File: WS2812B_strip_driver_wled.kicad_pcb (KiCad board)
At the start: 2 copper layers, 112.9 x 106.2 mm, 119 parts, among them J1 CH_1, J2 CH_2, J3 CH_3, J4 CH_4, J5 PWR_IN, J6 uPhone, J8 USB_C_Receptacle_USB2.0_16P, K1 RELAY_1, K2 RELAY_2, K3 RELAY_3, K4 RELAY_4, Q1 SS8050, Q2 SS8050, Q3 SS8050, Q4 SS8050, Q5 SS8050, Q6 SS8050, SW1 SW_EN, SW2 SW_IO0, U1 ESP32-WROOM-32E, U2 AMS1117-3.3, U3 CP2102N-Axx-xQFN28

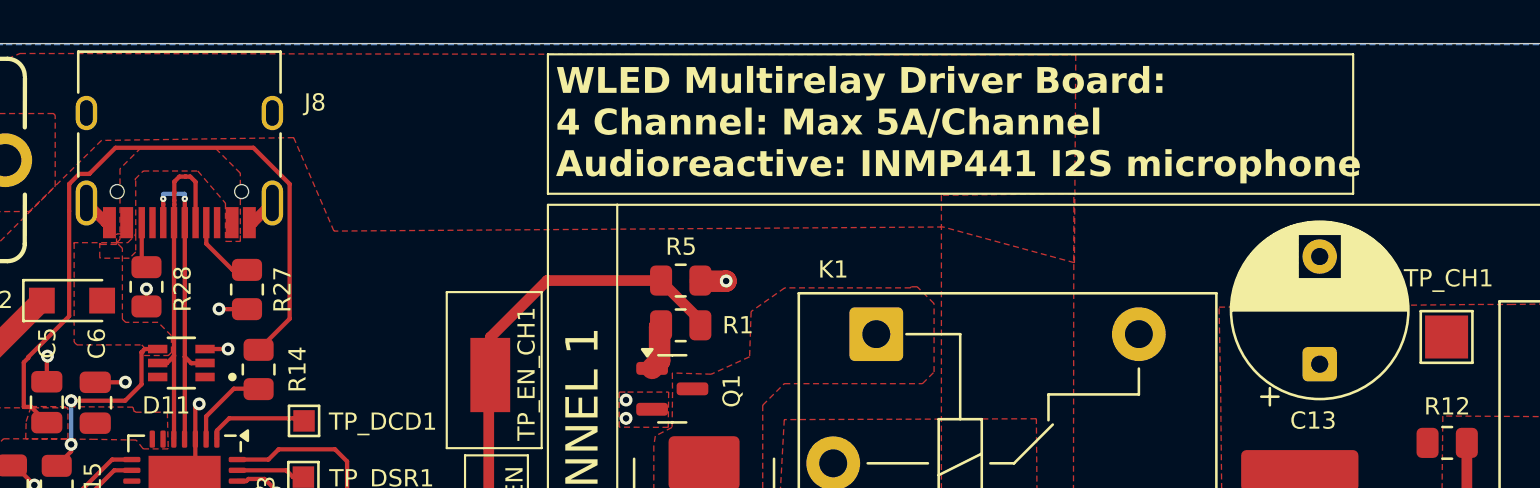
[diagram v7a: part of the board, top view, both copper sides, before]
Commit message: removed micro vias by usb-c connection
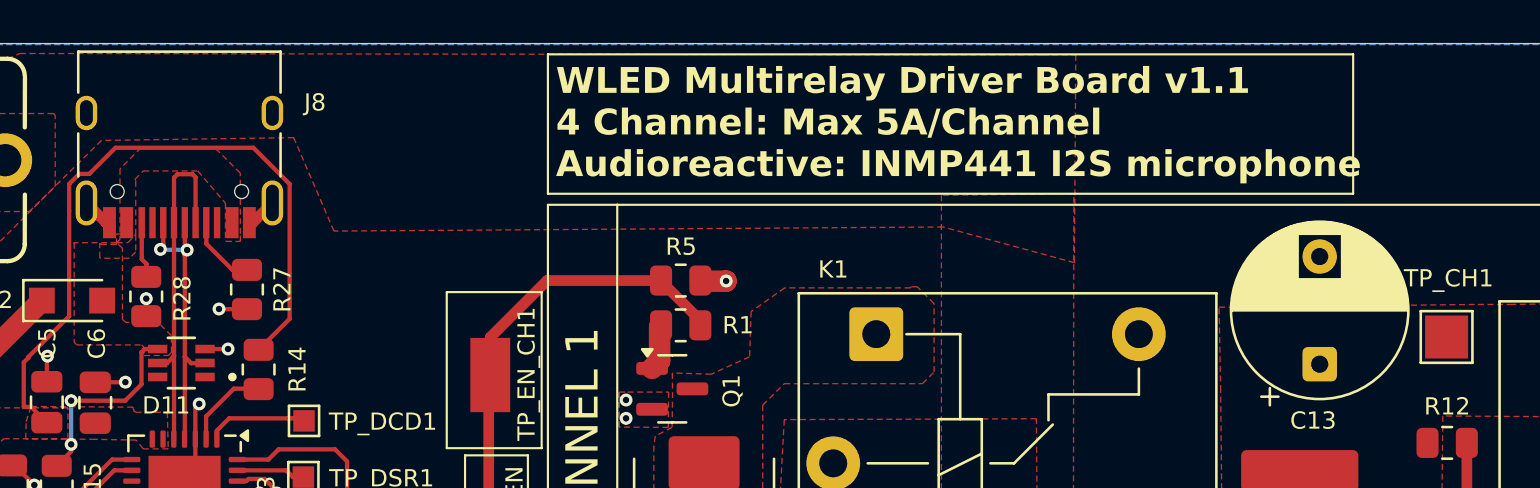
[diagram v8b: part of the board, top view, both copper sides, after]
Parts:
- moved R28 0.45 mm to (52.3, 85.7)
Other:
- board text added: "WLED Multirelay Driver Board v1.1 4 Channel: Max 5A/Channel Audioreactive: INMP441 I2S microphone"
- board text removed: "WLED Multirelay Driver Board: 4 Channel: Max 5A/Channel Audioreactive: INMP441 I2S microphone"
